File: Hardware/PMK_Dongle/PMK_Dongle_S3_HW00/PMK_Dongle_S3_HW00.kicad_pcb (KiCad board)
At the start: 4 copper layers, 10.4 x 15.4 mm, 37 parts, among them IC1 ESP32-S2FH4, J1 USB_A, U1 MIC5528-3.3YMT-T5, Y1 Crystal_GND24_Small

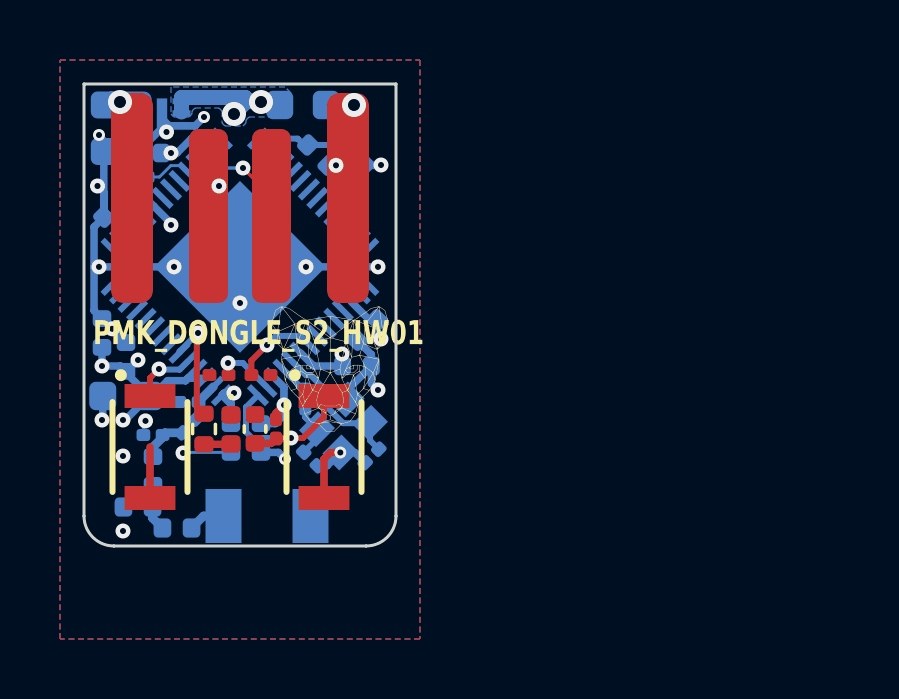
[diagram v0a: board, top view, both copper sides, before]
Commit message: started routing dongle_s3_00
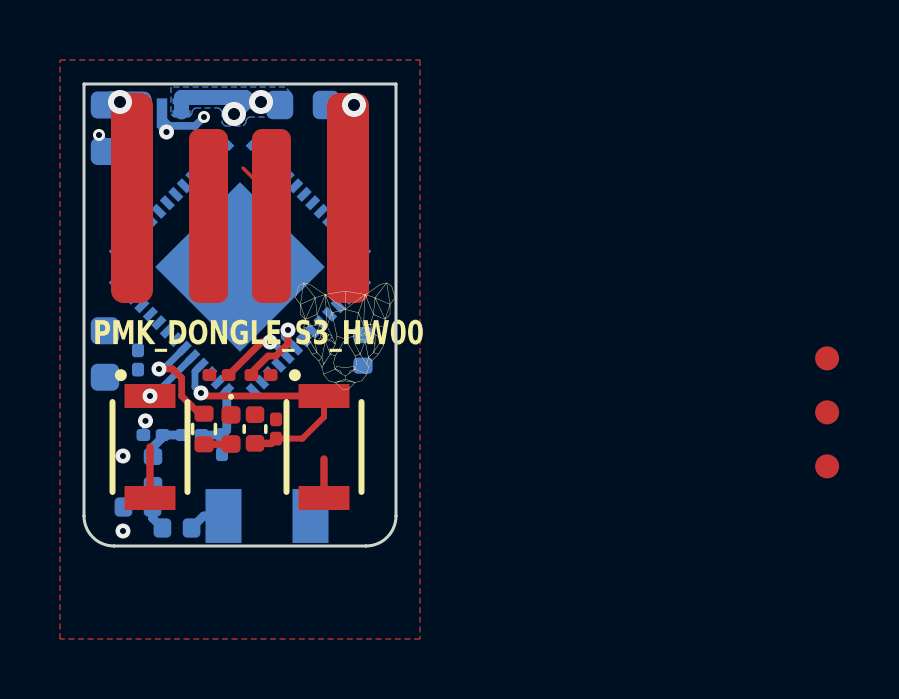
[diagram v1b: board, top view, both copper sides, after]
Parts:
- removed C11: 10u, Capacitor_SMD:C_0603_1608Metric
- removed C12, C15: 1u, Capacitor_SMD:C_0402_1005Metric
- removed C13, C14, C17, C18, C5, C6, C7, C8: 100n, Capacitor_SMD:C_0402_1005Metric
- removed C3, C4: 15p, Capacitor_SMD:C_0201_0603Metric
- removed IC1: ESP32-S2FH4, Component_lib:QFN40P700X700X90-57N-D
- removed R1: 0, Resistor_SMD:R_0201_0603Metric
- removed R3: 10k, Resistor_SMD:R_0201_0603Metric
- removed Y1: Crystal_GND24_Small, Component_lib:Crystal_SMD_2016-4Pin_2.0x1.6mm
- added C30: 22u, Capacitor_SMD:C_0603_1608Metric, B.Cu at (148.5, 42.2)
- added C31: 100n, Capacitor_SMD:C_0201_0603Metric, B.Cu at (149.6, 42.4)
- added R35: 499, Resistor_SMD:R_0402_1005Metric, B.Cu at (157.1, 42.1)
- added TP30: TestPoint, Component_lib:TestPoint_0.8mm, F.Cu at (172.6, 42.3)
- added TP31: TestPoint, Component_lib:TestPoint_0.8mm, F.Cu at (172.6, 44.1)
- added TP32: TestPoint, Component_lib:TestPoint_0.8mm, F.Cu at (172.6, 45.9)
- added U30: ESP32-S3FN8, Component_lib:ESP32-S3-PICO-1-N8R2, B.Cu at (153.0, 39.3)
- C40: renamed from C10; value C -> 1p2
- C41: renamed from C9; value C -> 1p8
- L40: renamed from L1; value L -> 2p7
- L41: renamed from L2; value 2.7n -> 2n7
- L42: renamed from L3; value 3.9n -> 3n9
- moved C40 1.80 mm to (152.4, 45.2), turned to -90 degrees
- moved G*** 1.21 mm to (156.5, 41.6)
- moved L40 0.32 mm to (151.4, 44.9), turned to 0 degrees
- renumbered ANT1 to ANT40, C1 to C20, C2 to C21, C16 to C32, C19 to C42, D1 to D30, J1 to J10, R4 to R30, R2 to R31, R5 to R33, R6 to R34, S1 to S30, S2 to S31, U1 to U20
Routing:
- net GND: track 46.6 -> 12.8 mm, vias 21 -> 7
- net +3V3: track 28.7 -> 5.21 mm, vias 11 -> 2
- net /QUARTZ_2: track 4.76 -> 0.00 mm
- net /VDD_SPI: track 2.78 -> 0.00 mm
- net /EN: track 6.36 -> 8.61 mm
- net /QUARTZ_1: track 1.80 -> 0.00 mm
- net /IO18: track 1.60 -> 0.00 mm
- net /D+: track 3.43 -> 1.99 mm, vias 1 -> 0
- net /D-: track 3.10 -> 2.04 mm, vias 1 -> 0
- net /QUARTZ_3: track 1.00 -> 0.00 mm
- net /LNA_IN: track 1.33 -> 2.23 mm
- net /IO46: track 2.02 -> 2.61 mm
- removed copper zone on B.Cu, net GND
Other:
- board text added: "PMK_DONGLE_S3_HW00"
- board text removed: "PMK_DONGLE_S2_HW01"
